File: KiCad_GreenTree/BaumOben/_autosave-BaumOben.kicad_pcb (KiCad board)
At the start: 2 copper layers, 73.4 x 99.4 mm, 42 parts

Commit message: BaumOben fertig
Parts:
- DB5, DB6, R9: moved to B.Cu
- moved DB8 96.6 mm to (90.4, 127.3)
- moved R10 91.2 mm to (90.6, 130.7)
- moved DB7 88.8 mm to (109.0, 80.8)
- moved DB6 78.6 mm to (107.2, 95.6)
- moved R9 71.5 mm to (108.5, 98.6)
- moved DB5 64.0 mm to (130.0, 124.4), turned to 180 degrees
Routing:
- net Net-(DB7-Pad1): track 0.00 -> 127.1 mm
- net Takt_invertiert_9V: track 54.8 -> 117.7 mm, vias 2 -> 4
- net Net-(DB3-Pad1): track 0.00 -> 53.9 mm, vias 0 -> 1
- net Net-(DB5-Pad1): track 0.00 -> 38.9 mm
- net Net-(DB1-Pad1): track 0.00 -> 26.6 mm, vias 0 -> 1
- net Takt_9V: track 90.3 -> 114.1 mm, vias 2 -> 4
- net Net-(DG6-Pad1): track 40.1 -> 33.9 mm
- net Net-(DB6-Pad1): track 0.00 -> 3.54 mm
- net Net-(DB8-Pad1): track 0.00 -> 3.51 mm
- net Net-(DB2-Pad1): track 0.00 -> 2.61 mm
- net Net-(DG5-Pad1): track 49.5 -> 50.2 mm
- net GND: vias 0 -> 7
- added copper zone on B.Cu, net (none)
- added copper zone on F.Cu, net (none)
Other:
- net class Supply added: clearance 0.2, trace_width 0.4, via_dia 0.8, via_drill 0.4

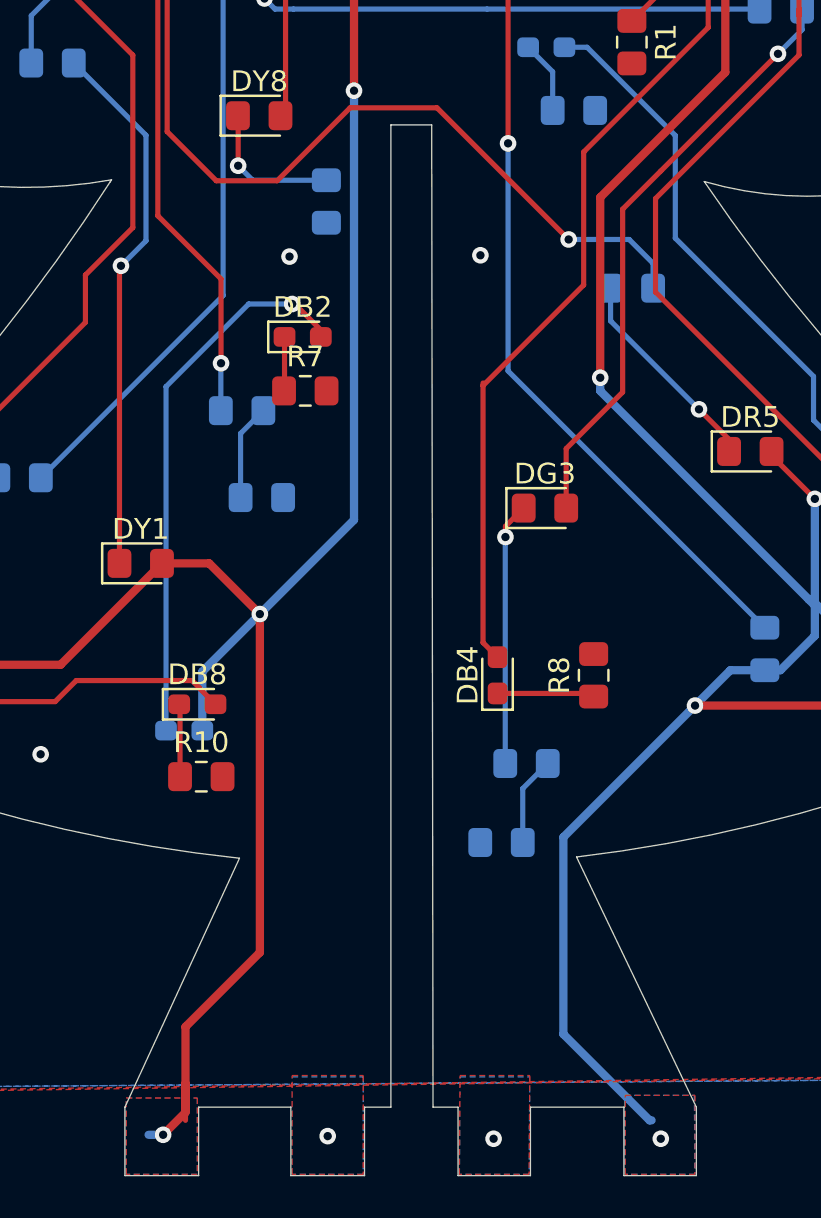
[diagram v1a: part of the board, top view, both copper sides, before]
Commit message: bis auf silk fertig
baum unten fertig gemacht und Beinchen gekürzt
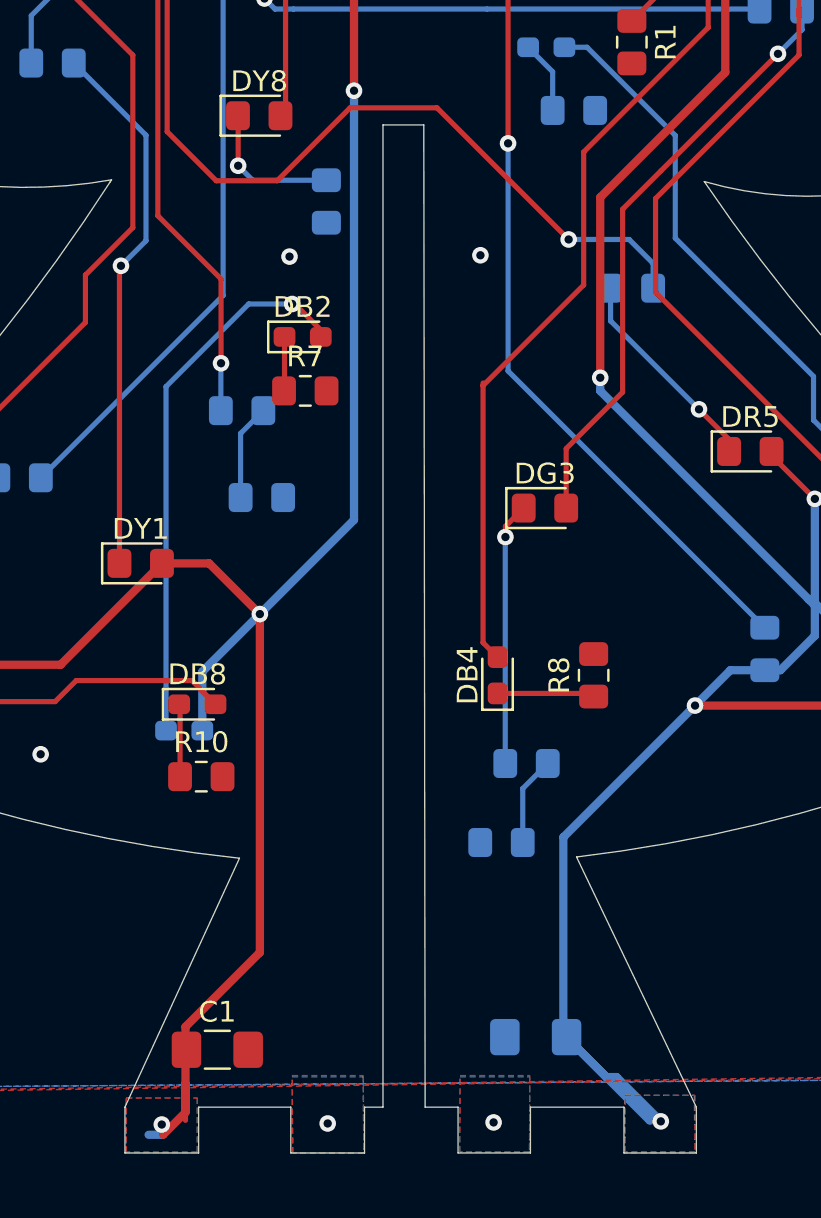
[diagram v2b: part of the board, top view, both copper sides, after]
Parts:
- added C1: 100n, Capacitor_SMD:C_1206_3216Metric_Pad1.42x1.75mm_HandSolder, F.Cu at (91.3, 143.9)
- added C2: 100n, Capacitor_SMD:C_1206_3216Metric_Pad1.42x1.75mm_HandSolder, B.Cu at (106.7, 143.3)
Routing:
- net Takt_invertiert_9V: track 117.7 -> 123.9 mm
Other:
- board size 73.4 x 99.4 mm -> 73.4 x 98.3 mm

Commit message: sterne auf silkscreen baum
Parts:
- added G***: LOGO, grafics:star_silk, B.Cu at (104.7, 63.5)
- added G***: LOGO, grafics:star_silk, B.Cu at (117.3, 100.1)
- added G***: LOGO, grafics:star_silk, B.Cu at (73.2, 124.5)
- added G***: LOGO, grafics:star_silk, B.Cu at (85.2, 111.3)
- added G***: LOGO, grafics:star_silk, B.Cu at (95.6, 126.2)
- added G***: LOGO, grafics:star_silk, B.Cu at (106.7, 109.6)
- added G***: LOGO, grafics:star_silk, B.Cu at (121.1, 129.1)
- added G***: LOGO, grafics:star_silk, B.Cu at (118.6, 114.3)
- added G***: LOGO, grafics:star_silk, F.Cu at (113.3, 119.6)
- added G***: LOGO, grafics:star_silk, F.Cu at (108.7, 131.5)
- added G***: LOGO, grafics:star_silk, F.Cu at (131.3, 125.0)
- added G***: LOGO, grafics:star_silk, B.Cu at (88.6, 73.5)
- added G***: LOGO, grafics:star_silk, F.Cu at (82.4, 127.1)
- added G***: LOGO, grafics:star_silk, F.Cu at (82.7, 116.6)
- added G***: LOGO, grafics:star_silk, F.Cu at (91.0, 115.1)
- added G***: LOGO, grafics:star_silk, F.Cu at (111.2, 85.4)
- added G***: LOGO, grafics:star_silk, F.Cu at (122.6, 99.1)
- added G***: LOGO, grafics:star_silk, F.Cu at (110.8, 107.5)
- added G***: LOGO, grafics:star_silk, F.Cu at (104.0, 91.6)
- added G***: LOGO, grafics:star_silk, F.Cu at (79.0, 99.5)
- added G***: LOGO, grafics:star_silk, F.Cu at (89.1, 95.9)
- added G***: LOGO, grafics:star_silk, F.Cu at (88.5, 85.5)
- added G***: LOGO, grafics:star_silk, B.Cu at (111.2, 72.0)
- added G***: LOGO, grafics:star_silk, F.Cu at (113.8, 74.2)
- added G***: LOGO, grafics:star_silk, F.Cu at (97.3, 60.2)
- added G***: LOGO, grafics:star_silk, F.Cu at (93.2, 68.5)
- added G***: LOGO, grafics:star_silk, B.Cu at (92.0, 80.9)
- added G***: LOGO, grafics:star_silk, B.Cu at (85.6, 89.9)
- added G***: LOGO, grafics:star_silk, B.Cu at (92.7, 96.6)
- added G***: LOGO, grafics:star_silk, B.Cu at (109.2, 82.5)
- added G***: LOGO, grafics:star_silk, B.Cu at (76.7, 99.0)
- added G***: LOGO, grafics:star_silk, B.Cu at (112.6, 92.2)
- turned R5 to 270 degrees
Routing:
- net Net-(DG4-Pad1): track 4.31 -> 5.42 mm
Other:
- outline, holes or cut-outs redrawn

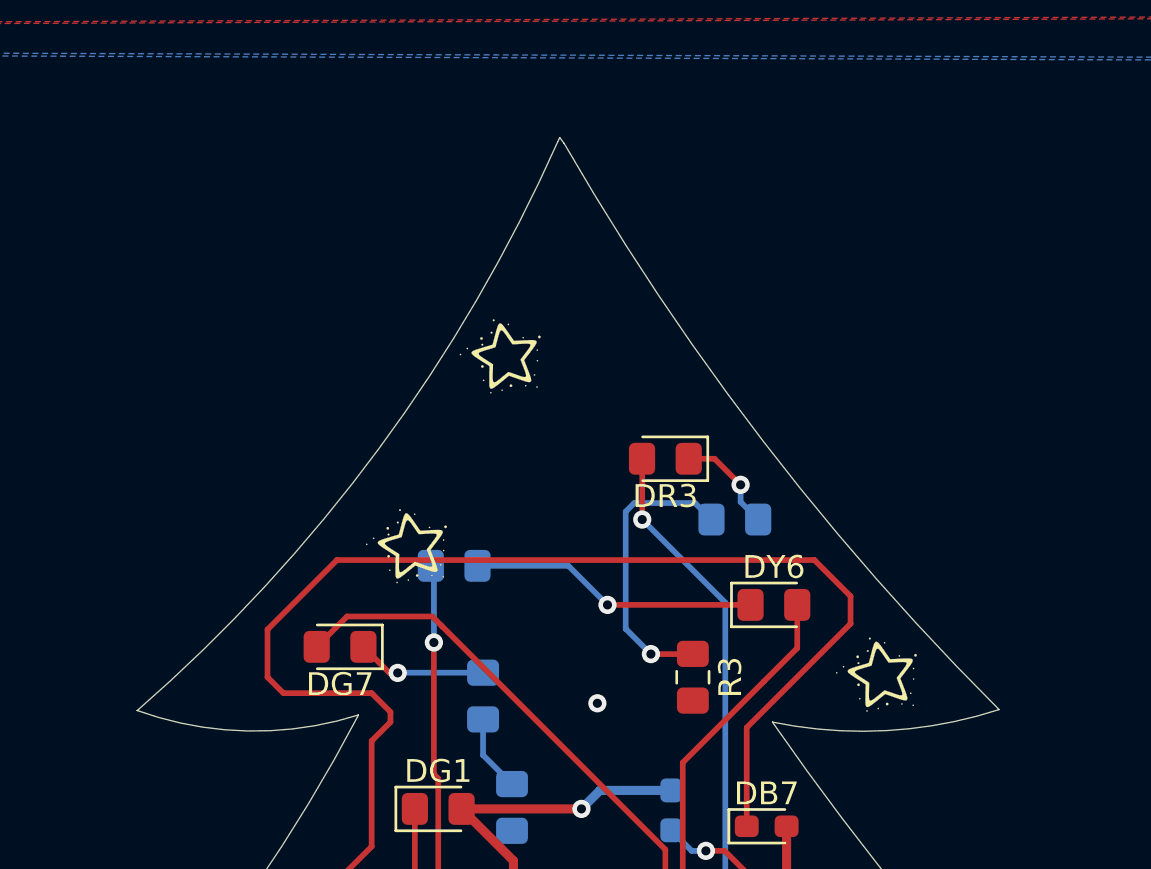
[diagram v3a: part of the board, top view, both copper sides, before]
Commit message: Schlitz korrigiert und Schrift Base
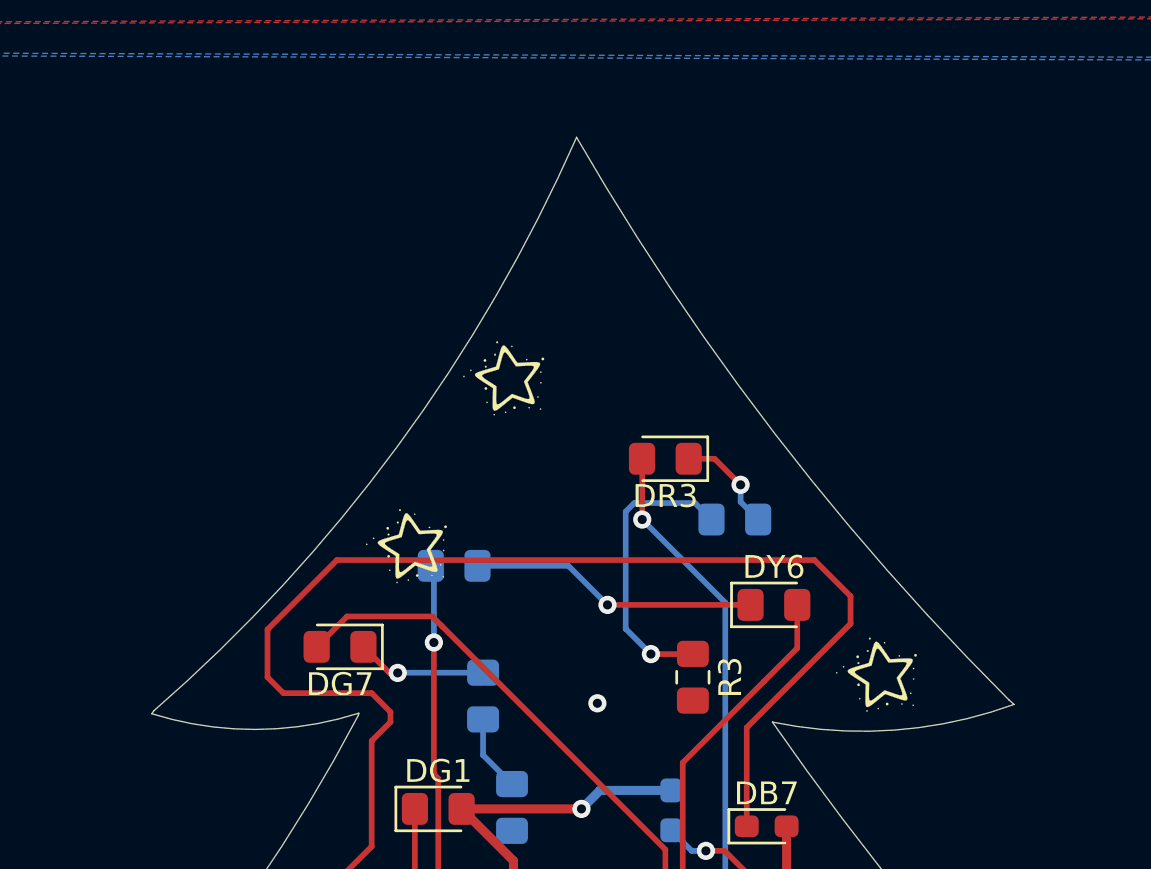
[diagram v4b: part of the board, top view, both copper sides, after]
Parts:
- moved G*** 0.98 mm to (97.5, 61.2)
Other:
- outline, holes or cut-outs redrawn

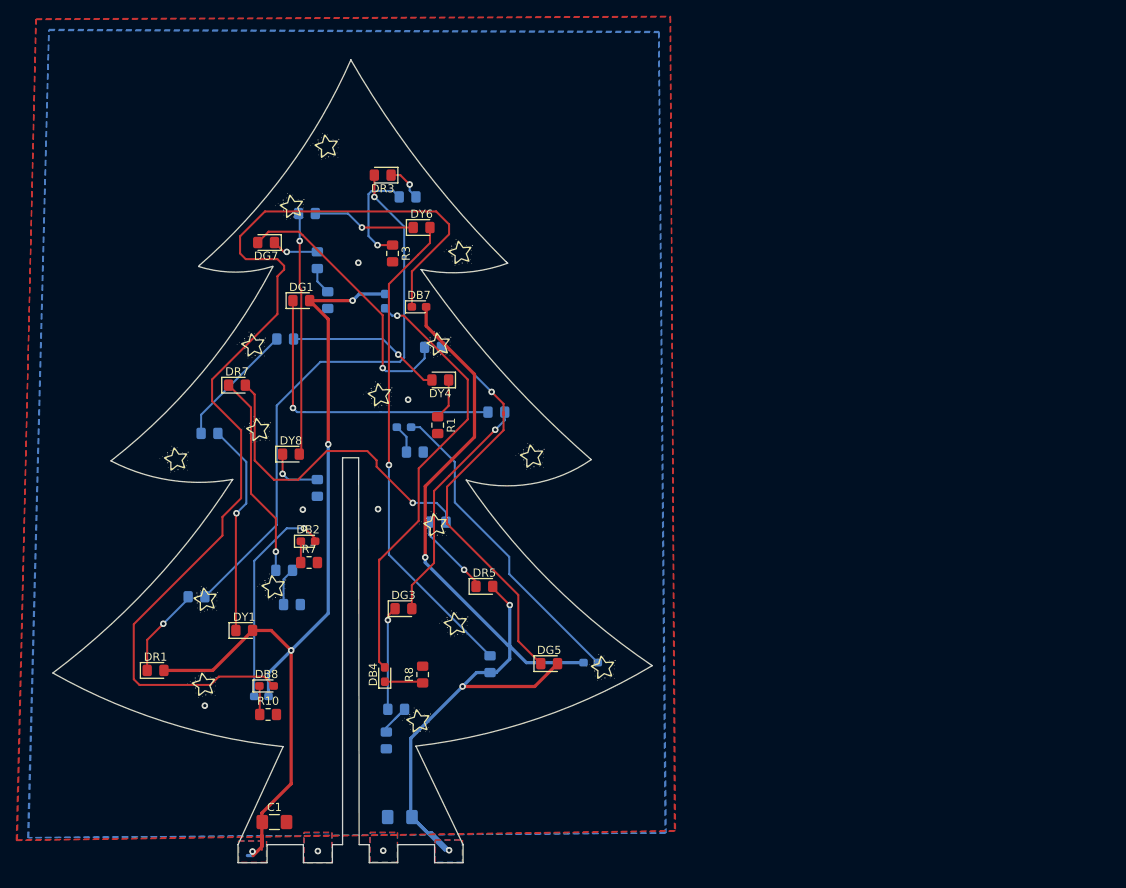
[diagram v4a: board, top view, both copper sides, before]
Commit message: edgecuts angepasst
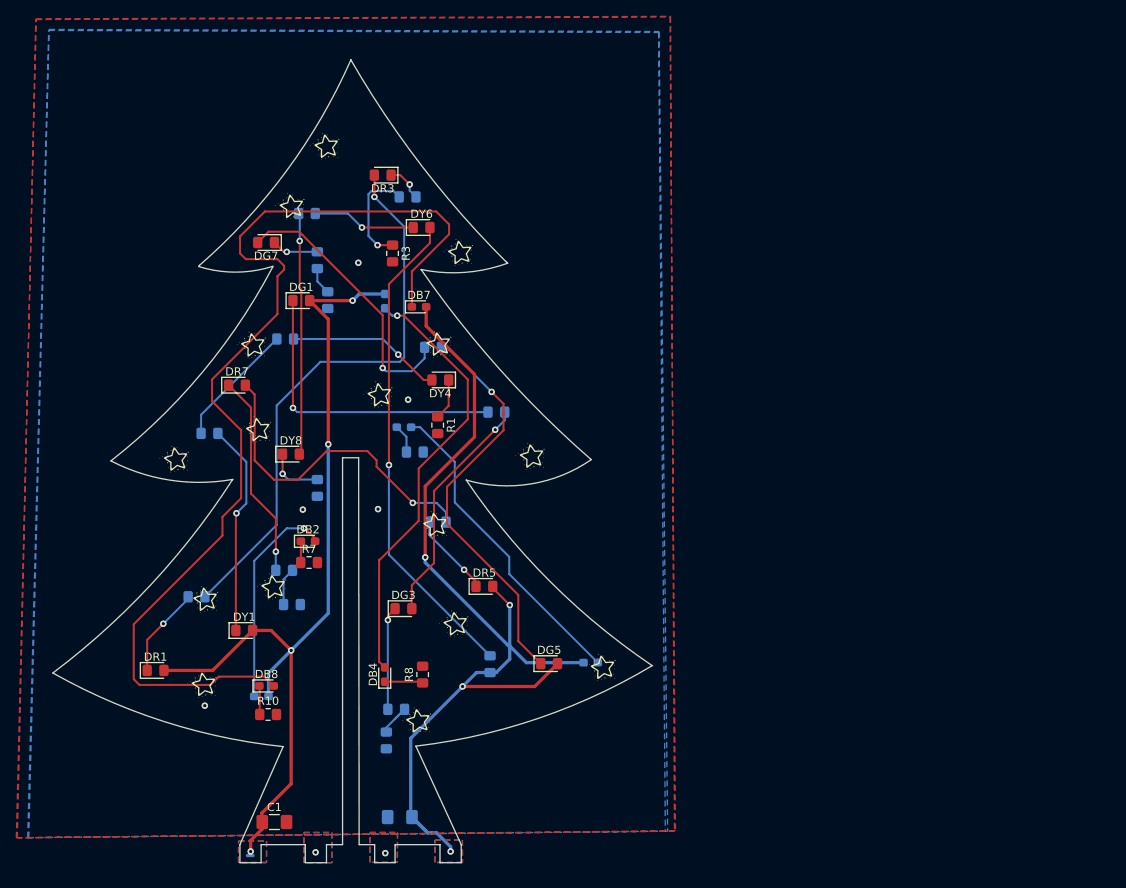
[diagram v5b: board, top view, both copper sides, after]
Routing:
- net Takt_9V: track 114.1 -> 108.0 mm
- net Takt_invertiert_9V: track 123.9 -> 121.5 mm
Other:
- outline, holes or cut-outs redrawn
